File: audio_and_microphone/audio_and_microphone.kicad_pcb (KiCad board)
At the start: 2 copper layers, 81.7 x 60.4 mm, 26 parts, among them J10 Conn_01x02_Pin, J4 Conn_01x03_Pin, J5 Conn_01x02, J7 Conn_01x02, J8 Conn_01x02, J9 Conn_01x02

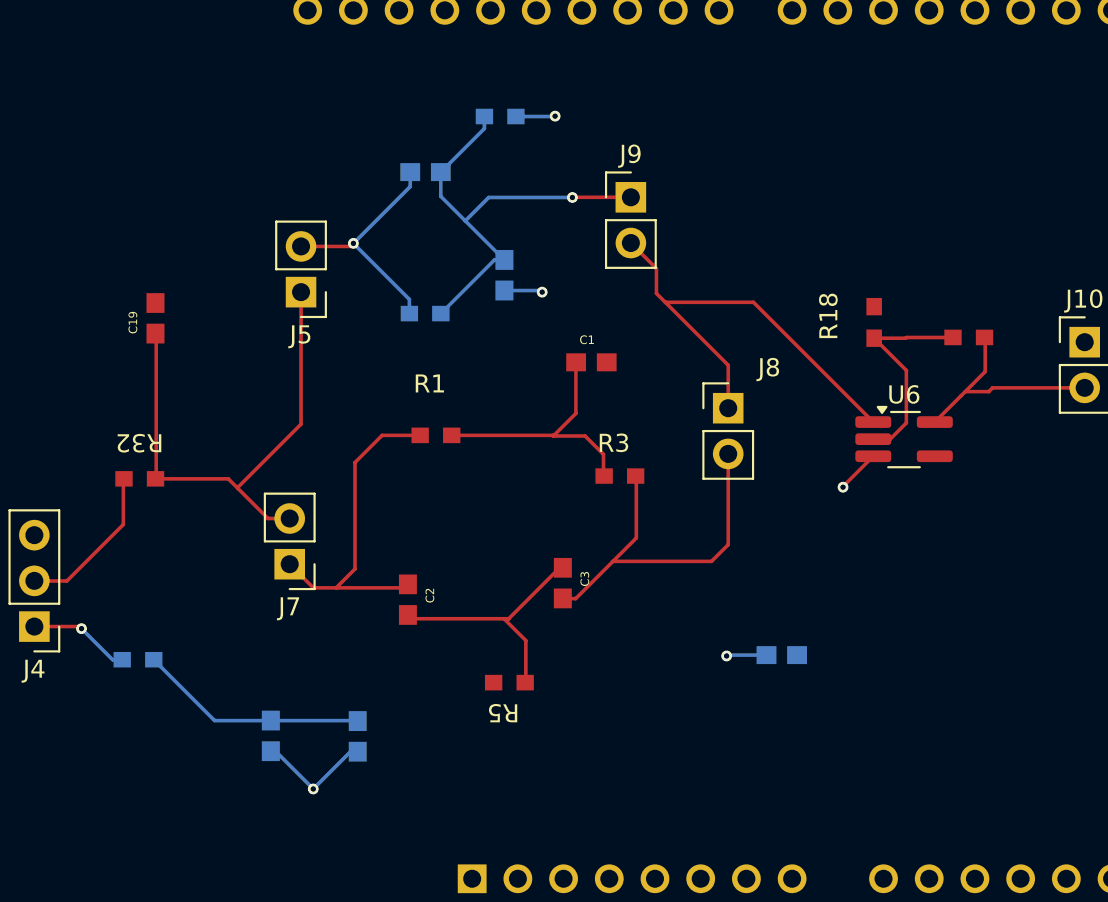
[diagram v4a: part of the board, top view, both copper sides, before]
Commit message: changed trace size and 90 degree angles
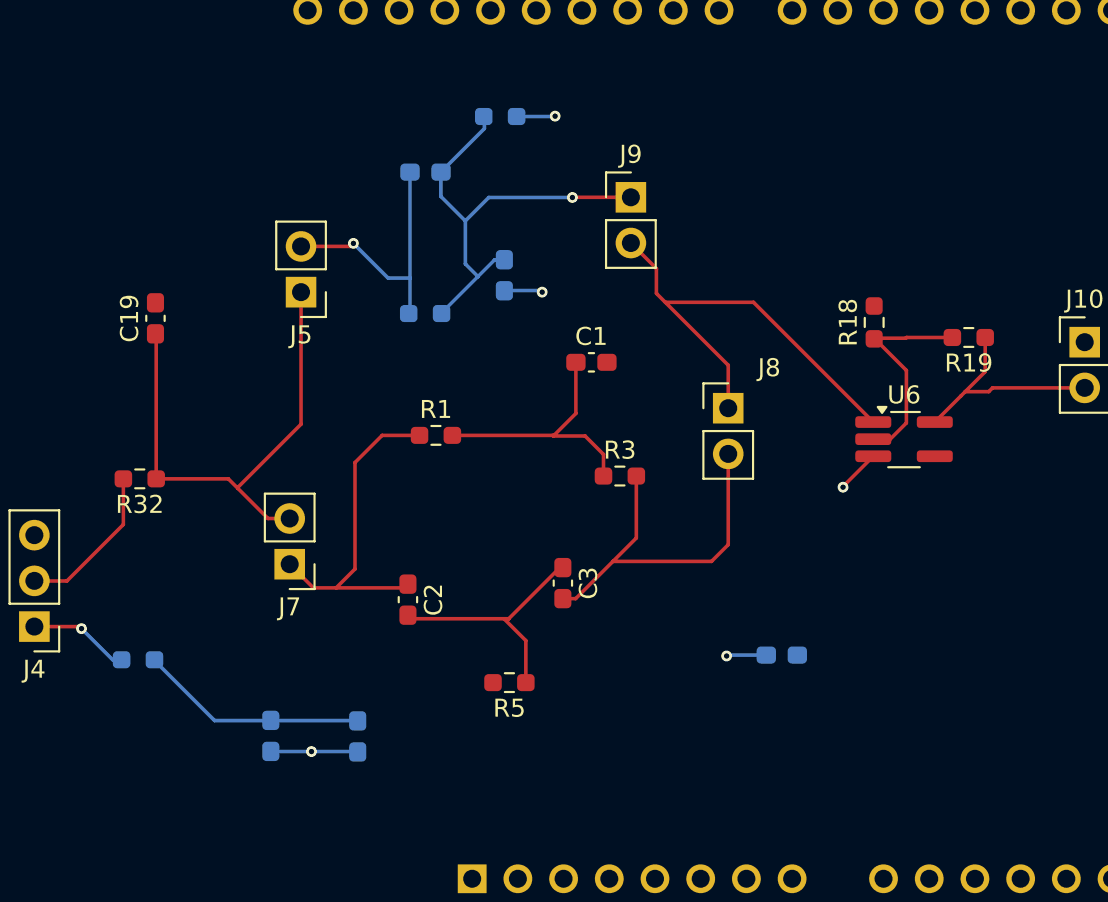
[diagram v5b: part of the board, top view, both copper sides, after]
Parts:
- C1, C14, C19, C2, C3, C4, C5, C6, C7: footprint C0603C104K5RACTU:CAPC1608X90 -> Capacitor_SMD:C_0603_1608Metric_Pad1.08x0.95mm_HandSolder
- R1, R18, R19, R3, R32, R5, R6, R7, R8: footprint Resistor1.60x0.80:RC0603N_YAG-M -> Resistor_SMD:R_0603_1608Metric_Pad0.98x0.95mm_HandSolder
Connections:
- A1 pad 4: +3.3V -> unconnected-(A1-3V3-Pad4)
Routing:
- net GND: track 13.1 -> 11.4 mm
- net Net-(J5-Pin_2): track 13.4 -> 14.8 mm

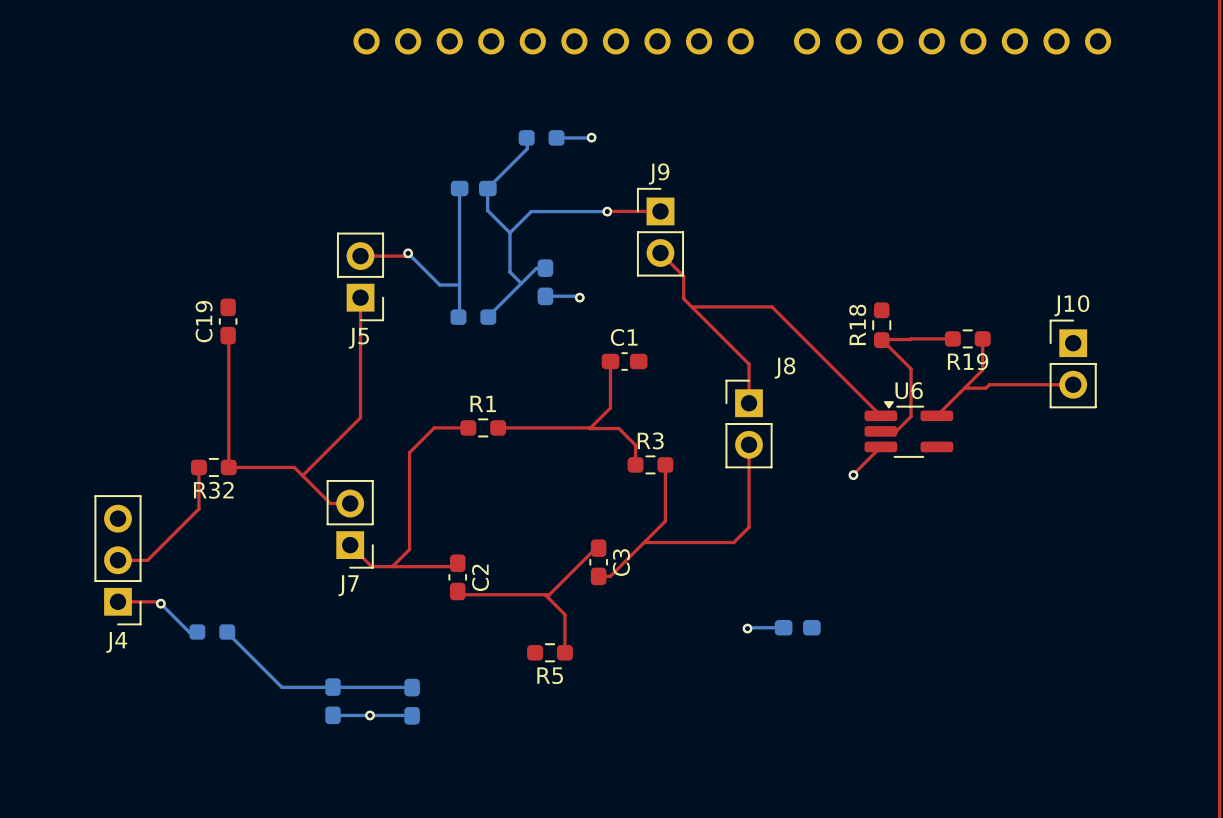
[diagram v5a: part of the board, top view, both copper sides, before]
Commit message: updated pcb to be cleaner with net labels and no redundancy
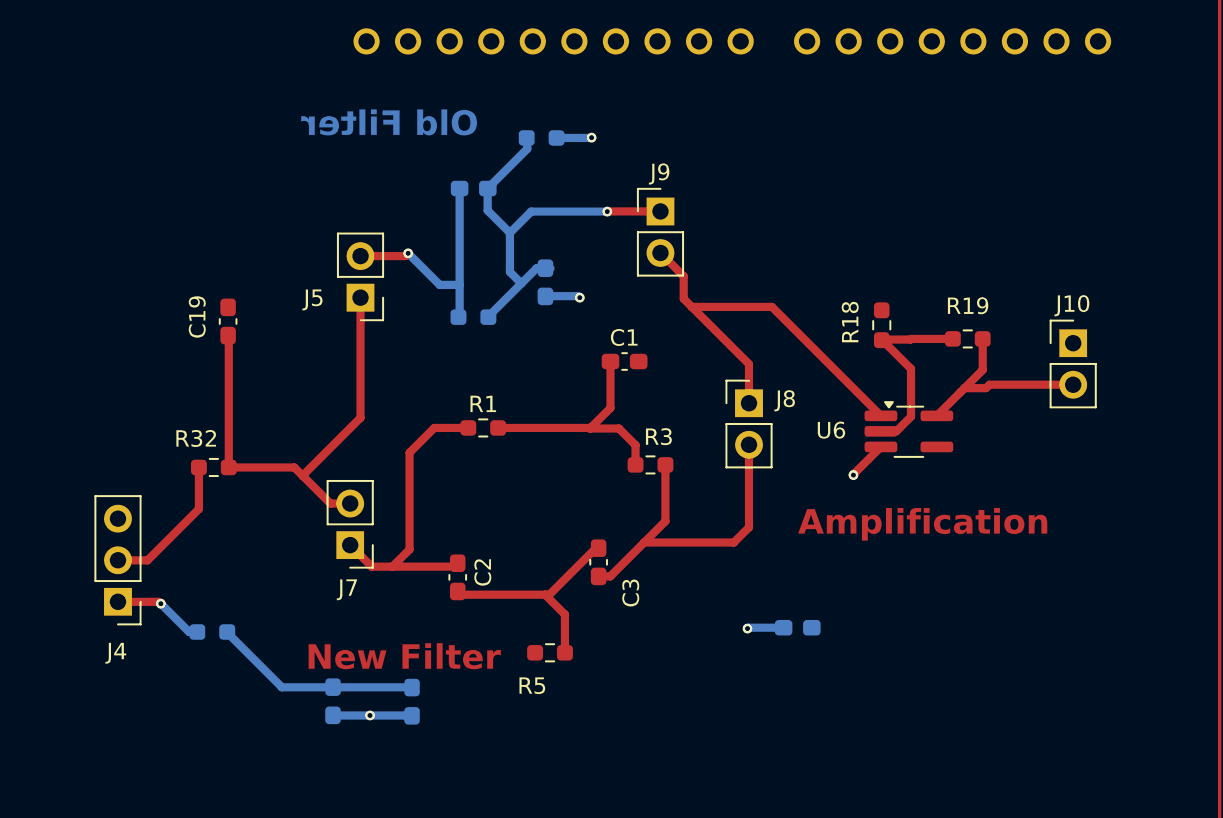
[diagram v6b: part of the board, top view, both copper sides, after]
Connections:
- net Net-(J5-Pin_1) renamed /before notch filter
- net Net-(J5-Pin_2) renamed /before old filter
- net Net-(J7-Pin_1) renamed /before new filter
- C3 pad 2: Net-(J8-Pin_2) -> /after new filter
- C6 pad 1: Net-(J9-Pin_1) -> /after new filter
- C7 pad 2: Net-(J9-Pin_1) -> /after new filter
- J4 pad 1: Net-(J4-Pin_1) -> +3.3V
- R3 pad 2: Net-(J8-Pin_2) -> /after new filter
- R7 pad 2: Net-(J9-Pin_1) -> /after new filter
- R8 pad 1: Net-(J9-Pin_1) -> /after new filter
- U6 pad 1: Net-(J8-Pin_1) -> /after new filter
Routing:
- net Net-(J9-Pin_1): vias 1 -> 0
- net Net-(J4-Pin_1): vias 1 -> 0
- net /after new filter: vias 0 -> 1
- net +3.3V: vias 1 -> 2
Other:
- board text added: "Amplification"
- board text added: "New Filter"
- board text added: "Old Filter"
